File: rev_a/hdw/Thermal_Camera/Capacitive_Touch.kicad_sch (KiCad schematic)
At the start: 24 parts, among them SW2901 Cap_Touch, SW2902 Cap_Touch, U2901 AT42QT1010-TSHR, U2902 AT42QT1010-TSHR, U2903 74LVC1G97, U2904 74LVC1G97

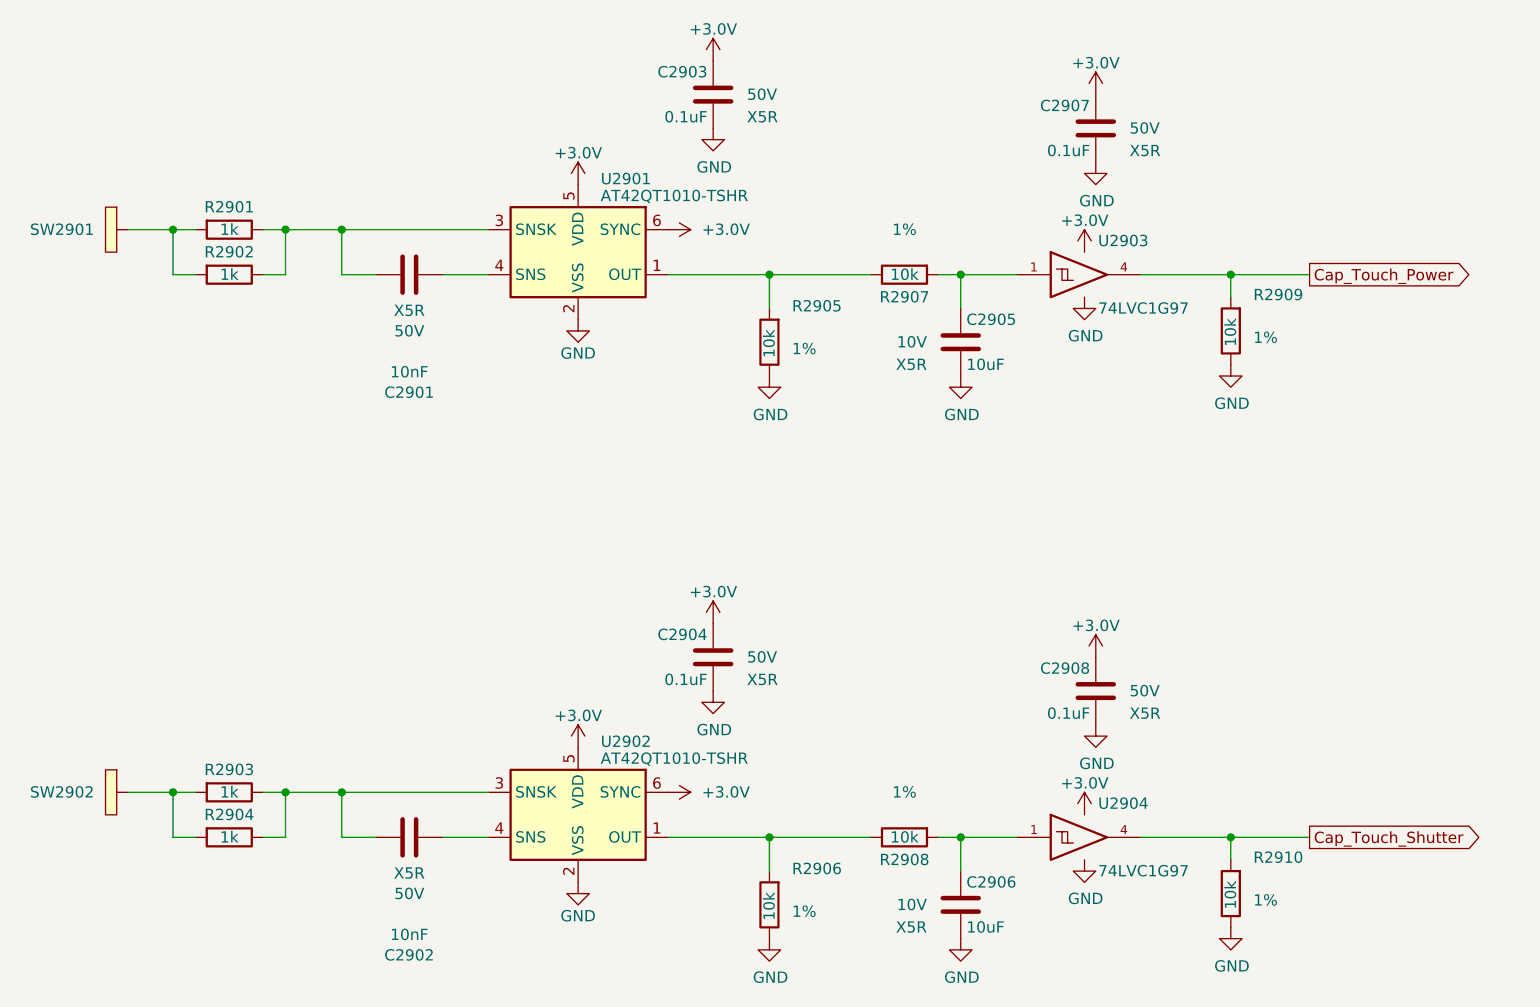
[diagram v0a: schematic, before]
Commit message: assigned a ton of footprints
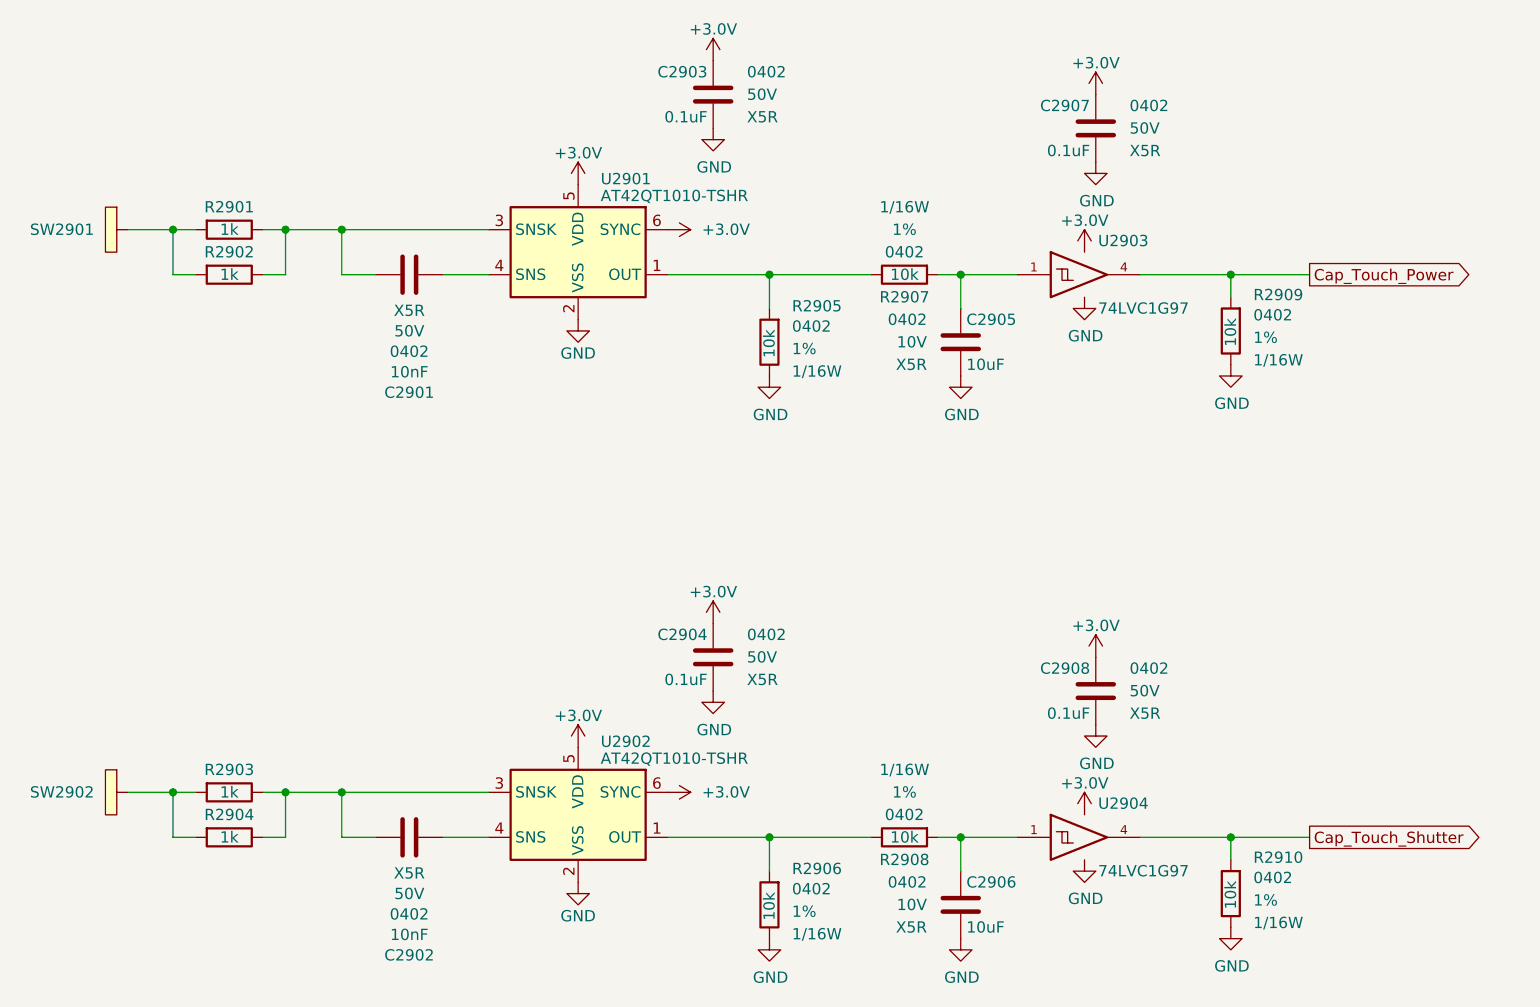
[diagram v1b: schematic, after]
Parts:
- C2901, C2902, C2903, C2904, C2905, C2906, C2907, C2908: footprint (none) -> Capacitors_SMD:C_0402; display_footprint (none) -> 0402
- R2901, R2902, R2903, R2904, R2905, R2906, R2907, R2908, R2909, R2910: footprint (none) -> Resistors_SMD:R_0402; Wattage (none) -> 1/16W; display_footprint (none) -> 0402
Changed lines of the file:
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@@
 			)
 		)
-		(property "Footprint" ""
+		(property "Footprint" "Capacitors_SMD:C_0402"
 			(at 136.8552 58.42 0)
 			(effects
@@
 			)
 		)
-		(property "display_footprint" ""
+		(property "display_footprint" "0402"
 			(at 132.08 52.07 0)
 			(effects
@@
 			)
 		)
-		(property "Footprint" ""
+		(property "Footprint" "Capacitors_SMD:C_0402"
 			(at 69.85 109.5248 0)
 			(effects
@@
 			)
 		)
-		(property "display_footprint" ""
+		(property "display_footprint" "0402"
 			(at 73.66 119.1768 90)
 			(effects
@@
 			)
 		)
-		(property "Footprint" ""
+		(property "Footprint" "Resistors_SMD:R_0402"
 			(at 53.34 110.49 0)
 			(effects
@@
 			)
 		)
-		(property "display_footprint" ""
+		(property "display_footprint" "0402"
 			(at 51.562 107.95 0)
 			(effects
@@
 			)
 		)
-		(property "Wattage" ""
+		(property "Wattage" "1/16W"
 			(at 56.642 107.95 0)
 			(effects
@@
 			)
 		)
-		(property "Footprint" ""
+		(property "Footprint" "Resistors_SMD:R_0402"
 			(at 53.34 105.41 0)
 			(effects
@@
 			)
 		)
-		(property "display_footprint" ""
+		(property "display_footprint" "0402"
 			(at 51.562 102.87 0)
 			(effects
@@
 			)
 		)
-		(property "Wattage" ""
+		(property "Wattage" "1/16W"
 			(at 56.642 102.87 0)
 			(effects
@@
 			)
 		)
-		(property "Footprint" ""
+		(property "Footprint" "Resistors_SMD:R_0402"
 			(at 114.3 54.61 0)
 			(effects
@@
 			)
 		)
-		(property "display_footprint" ""
+		(property "display_footprint" "0402"
 			(at 116.84 52.832 0)
 			(effects
@@
 			)
 		)
-		(property "Wattage" ""
+		(property "Wattage" "1/16W"
 			(at 116.84 57.912 0)
 			(effects
@@
 			)
 		)
-		(property "Footprint" ""
+		(property "Footprint" "Resistors_SMD:R_0402"
 			(at 166.37 116.84 0)
 			(effects
@@
 			)
 		)
-		(property "display_footprint" ""
+		(property "display_footprint" "0402"
 			(at 168.91 115.062 0)
 			(effects
@@
 			)
 		)
-		(property "Wattage" ""
+		(property "Wattage" "1/16W"
 			(at 168.91 120.142 0)
 			(effects
@@
 			)
 		)
-		(property "Footprint" ""
+		(property "Footprint" "Resistors_SMD:R_0402"
 			(at 166.37 53.34 0)
 			(effects
@@
 			)
 		)
-		(property "display_footprint" ""
+		(property "display_footprint" "0402"
 			(at 168.91 51.562 0)
 			(effects
@@
 			)
 		)
-		(property "Wattage" ""
+		(property "Wattage" "1/16W"
 			(at 168.91 56.642 0)
 			(effects
@@
 			)
 		)
-		(property "Footprint" ""
+		(property "Footprint" "Capacitors_SMD:C_0402"
 			(at 150.1648 97.79 0)
 			(effects
@@
 			)
 		)
-		(property "display_footprint" ""
+		(property "display_footprint" "0402"
 			(at 154.94 91.44 0)
 			(effects
@@
 			)
 		)
-		(property "Footprint" ""
+		(property "Footprint" "Resistors_SMD:R_0402"
 			(at 114.3 118.11 0)
 			(effects
@@
 			)
 		)
-		(property "display_footprint" ""
+		(property "display_footprint" "0402"
 			(at 116.84 116.332 0)
 			(effects
@@
 			)
 		)
-		(property "Wattage" ""
+		(property "Wattage" "1/16W"
 			(at 116.84 121.412 0)
 			(effects
@@
 			)
 		)
-		(property "Footprint" ""
+		(property "Footprint" "Resistors_SMD:R_0402"
 			(at 53.34 46.99 0)
 			(effects
@@
 			)
 		)
-		(property "display_footprint" ""
+		(property "display_footprint" "0402"
 			(at 51.562 44.45 0)
 			(effects
@@
 			)
 		)
-		(property "Wattage" ""
+		(property "Wattage" "1/16W"
 			(at 56.642 44.45 0)
 			(effects
@@
 			)
 		)
-		(property "Footprint" ""
+		(property "Footprint" "Resistors_SMD:R_0402"
 			(at 129.54 46.99 0)
 			(effects
@@
 			)
 		)
-		(property "display_footprint" ""
+		(property "display_footprint" "0402"
 			(at 129.54 44.45 90)
 			(effects
@@
 			)
 		)
-		(property "Wattage" ""
+		(property "Wattage" "1/16W"
 			(at 129.54 39.37 90)
 			(effects
@@
 			)
 		)
-		(property "Footprint" ""
+		(property "Footprint" "Resistors_SMD:R_0402"
 			(at 129.54 110.49 0)
 			(effects
@@
 			)
 		)
-		(property "display_footprint" ""
+		(property "display_footprint" "0402"
 			(at 129.54 107.95 90)
 			(effects
@@
 			)
 		)
-		(property "Wattage" ""
+		(property "Wattage" "1/16W"
 			(at 129.54 102.87 90)
 			(effects
@@
 			)
 		)
-		(property "Footprint" ""
+		(property "Footprint" "Capacitors_SMD:C_0402"
 			(at 150.1648 34.29 0)
 			(effects
@@
 			)
 		)
-		(property "display_footprint" ""
+		(property "display_footprint" "0402"
 			(at 154.94 27.94 0)
 			(effects
@@
 			)
 		)
-		(property "Footprint" ""
+		(property "Footprint" "Capacitors_SMD:C_0402"
 			(at 106.9848 93.98 0)
 			(effects
@@
 			)
 		)
-		(property "display_footprint" ""
+		(property "display_footprint" "0402"
 			(at 111.76 87.63 0)
 			(effects
@@
 			)
 		)
-		(property "Footprint" ""
+		(property "Footprint" "Capacitors_SMD:C_0402"
 			(at 69.85 46.0248 0)
 			(effects
@@
 			)
 		)
-		(property "display_footprint" ""
+		(property "display_footprint" "0402"
 			(at 73.66 55.6768 90)
 			(effects
@@
 			)
 		)
-		(property "Footprint" ""
+		(property "Footprint" "Resistors_SMD:R_0402"
 			(at 53.34 41.91 0)
 			(effects
@@
 			)
 		)
-		(property "display_footprint" ""
+		(property "display_footprint" "0402"
 			(at 51.562 39.37 0)
 			(effects
@@
 			)
 		)
-		(property "Wattage" ""
+		(property "Wattage" "1/16W"
 			(at 56.642 39.37 0)
 			(effects
@@
 			)
 		)
-		(property "Footprint" ""
+		(property "Footprint" "Capacitors_SMD:C_0402"
 			(at 136.8552 121.92 0)
 			(effects
@@
 			)
 		)
-		(property "display_footprint" ""
+		(property "display_footprint" "0402"
 			(at 132.08 115.57 0)
 			(effects
@@
 			)
 		)
-		(property "Footprint" ""
+		(property "Footprint" "Capacitors_SMD:C_0402"
 			(at 106.9848 30.48 0)
 			(effects
@@
 			)
 		)
-		(property "display_footprint" ""
+		(property "display_footprint" "0402"
 			(at 111.76 24.13 0)
 			(effects

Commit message: assigned some part numbers
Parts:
- C2901, C2902: Digi-Key PN (none) -> 445-12201-1-ND
- C2903, C2904, C2907, C2908: Digi-Key PN (none) -> 490-10697-1-ND
- C2905, C2906: Digi-Key PN (none) -> 490-GRM155R61A106ME11DCT-ND
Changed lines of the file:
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@@
 			)
 		)
-		(property "Digi-Key PN" ""
+		(property "Digi-Key PN" "490-GRM155R61A106ME11DCT-ND"
 			(at 146.685 41.91 0)
 			(effects
@@
 			)
 		)
-		(property "Digi-Key PN" ""
+		(property "Digi-Key PN" "445-12201-1-ND"
 			(at 17.272 232.156 0)
 			(effects
@@
 			)
 		)
-		(property "Digi-Key PN" ""
+		(property "Digi-Key PN" "490-10697-1-ND"
 			(at 140.335 81.28 0)
 			(effects
@@
 			)
 		)
-		(property "Digi-Key PN" ""
+		(property "Digi-Key PN" "490-10697-1-ND"
 			(at 140.335 17.78 0)
 			(effects
@@
 			)
 		)
-		(property "Digi-Key PN" ""
+		(property "Digi-Key PN" "490-10697-1-ND"
 			(at 97.155 77.47 0)
 			(effects
@@
 			)
 		)
-		(property "Digi-Key PN" ""
+		(property "Digi-Key PN" "445-12201-1-ND"
 			(at 17.272 168.656 0)
 			(effects
@@
 			)
 		)
-		(property "Digi-Key PN" ""
+		(property "Digi-Key PN" "490-GRM155R61A106ME11DCT-ND"
 			(at 146.685 105.41 0)
 			(effects
@@
 			)
 		)
-		(property "Digi-Key PN" ""
+		(property "Digi-Key PN" "490-10697-1-ND"
 			(at 97.155 13.97 0)
 			(effects

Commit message: assigned resistor part numbers
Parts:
- R2901, R2902, R2903, R2904: Digi-Key PN (none) -> RMCF0402FT1K00CT-ND
- R2905, R2906, R2907, R2908, R2909, R2910: Digi-Key PN (none) -> RMCF0402FT10K0CT-ND
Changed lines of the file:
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@@
 			)
 		)
-		(property "Digi-Key PN" ""
+		(property "Digi-Key PN" "RMCF0402FT1K00CT-ND"
 			(at 43.18 102.87 0)
 			(effects
@@
 			)
 		)
-		(property "Digi-Key PN" ""
+		(property "Digi-Key PN" "RMCF0402FT1K00CT-ND"
 			(at 43.18 97.79 0)
 			(effects
@@
 			)
 		)
-		(property "Digi-Key PN" ""
+		(property "Digi-Key PN" "RMCF0402FT10K0CT-ND"
 			(at 121.92 44.45 0)
 			(effects
@@
 			)
 		)
-		(property "Digi-Key PN" ""
+		(property "Digi-Key PN" "RMCF0402FT10K0CT-ND"
 			(at 173.99 106.68 0)
 			(effects
@@
 			)
 		)
-		(property "Digi-Key PN" ""
+		(property "Digi-Key PN" "RMCF0402FT10K0CT-ND"
 			(at 173.99 43.18 0)
 			(effects
@@
 			)
 		)
-		(property "Digi-Key PN" ""
+		(property "Digi-Key PN" "RMCF0402FT10K0CT-ND"
 			(at 121.92 107.95 0)
 			(effects
@@
 			)
 		)
-		(property "Digi-Key PN" ""
+		(property "Digi-Key PN" "RMCF0402FT1K00CT-ND"
 			(at 43.18 39.37 0)
 			(effects
@@
 			)
 		)
-		(property "Digi-Key PN" ""
+		(property "Digi-Key PN" "RMCF0402FT10K0CT-ND"
 			(at 129.54 46.99 0)
 			(effects
@@
 			)
 		)
-		(property "Digi-Key PN" ""
+		(property "Digi-Key PN" "RMCF0402FT10K0CT-ND"
 			(at 129.54 110.49 0)
 			(effects
@@
 			)
 		)
-		(property "Digi-Key PN" ""
+		(property "Digi-Key PN" "RMCF0402FT1K00CT-ND"
 			(at 43.18 34.29 0)
 			(effects
